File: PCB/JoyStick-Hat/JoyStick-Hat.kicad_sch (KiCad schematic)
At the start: 0 parts

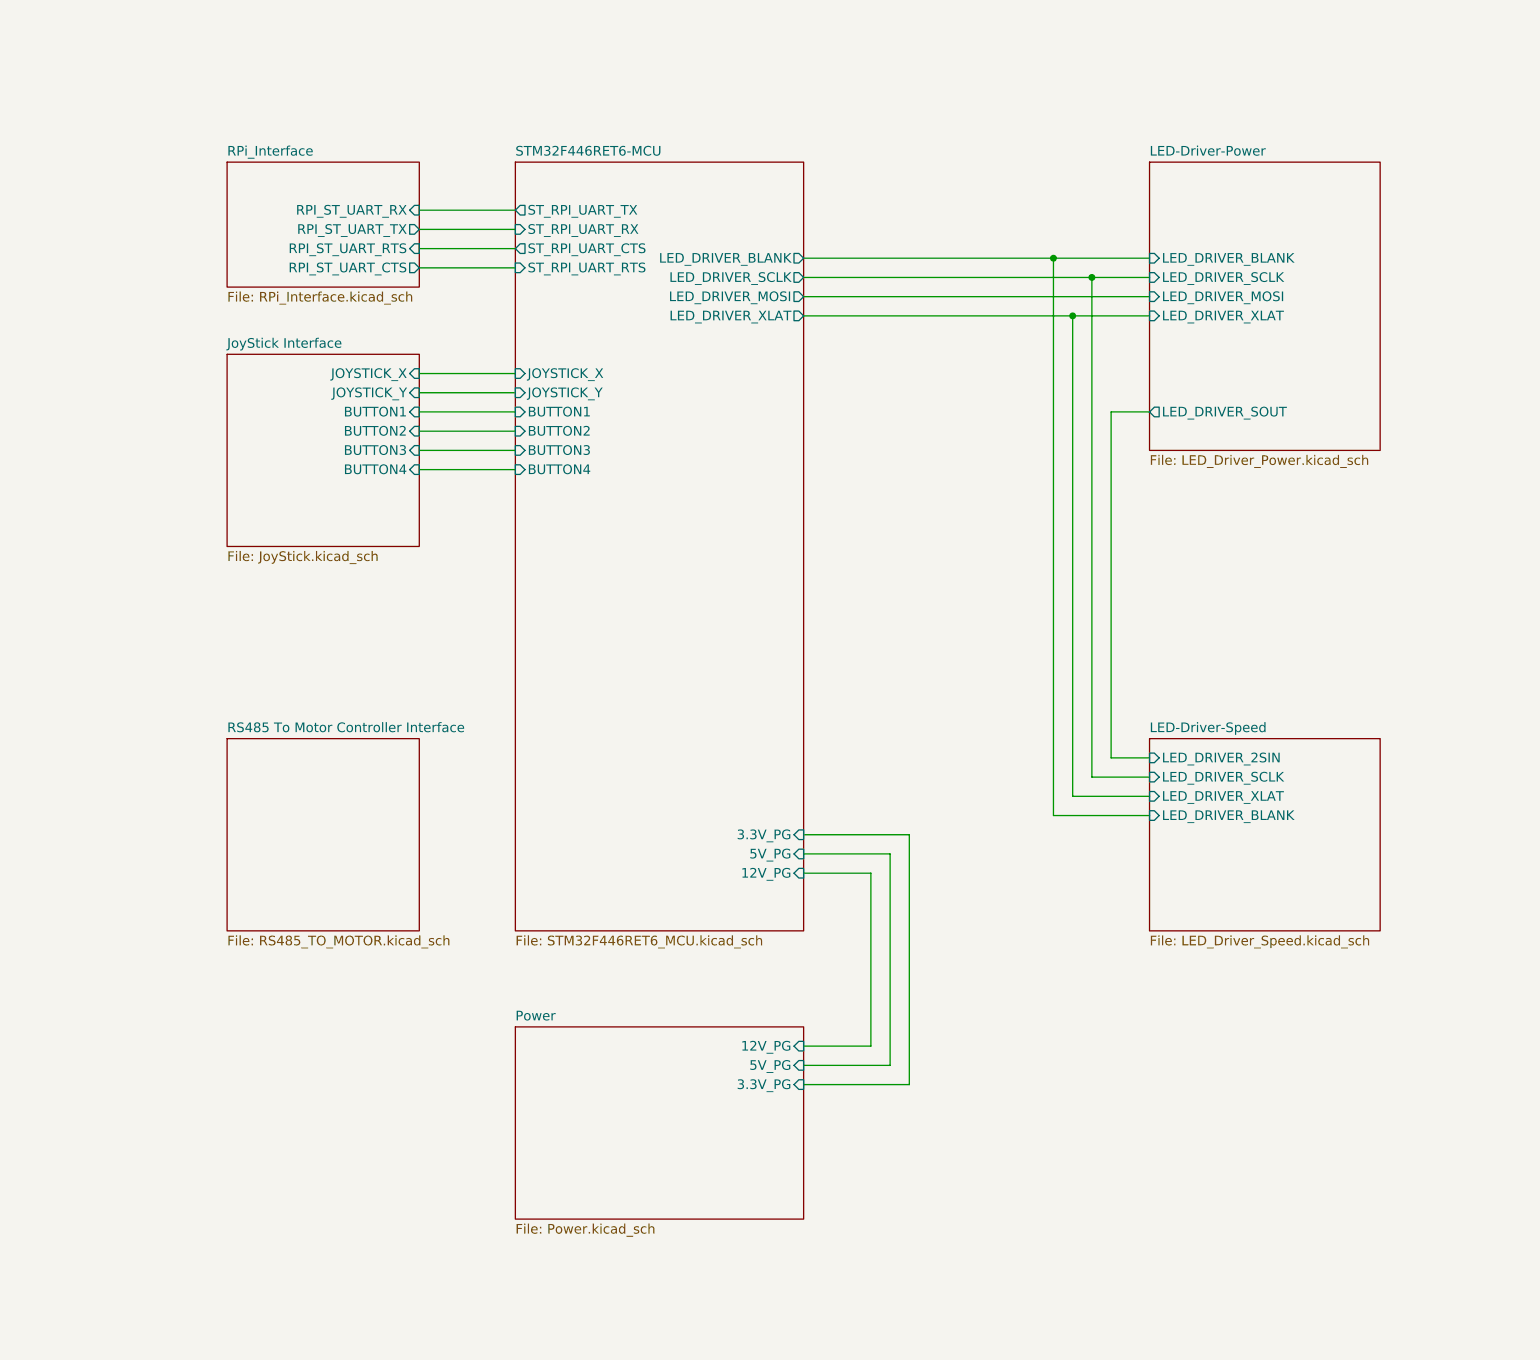
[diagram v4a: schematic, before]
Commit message: Schematic Complete
Schematic completed. Moved to 100 pin version of STM32 MCU for more connectivity and better muxing of internal peripherals with pins.
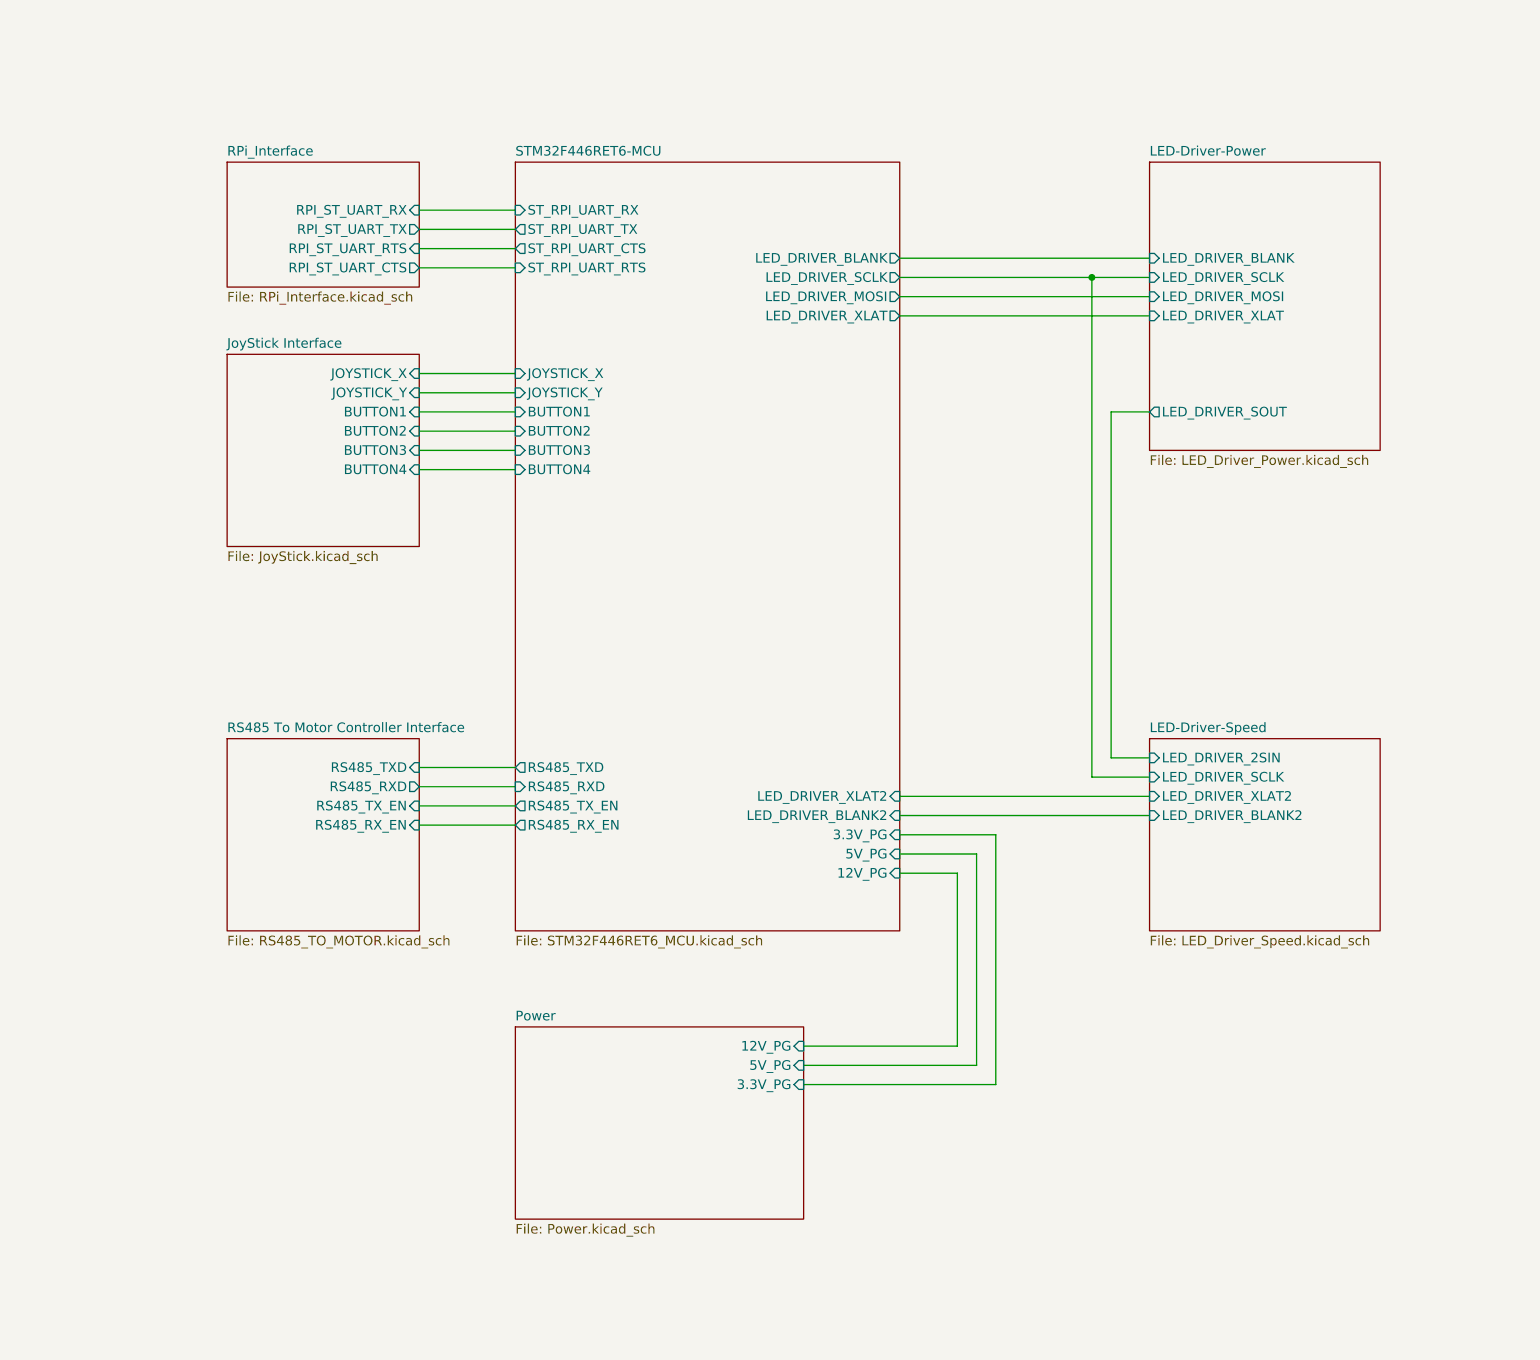
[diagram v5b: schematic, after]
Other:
- sheet LED-Driver-Speed ports: added LED_DRIVER_BLANK2, LED_DRIVER_XLAT2; removed LED_DRIVER_BLANK, LED_DRIVER_XLAT
- sheet RS485 To Motor Controller Interface ports: added RS485_RXD, RS485_RX_EN, RS485_TXD, RS485_TX_EN; removed none
- sheet STM32F446RET6-MCU ports: added LED_DRIVER_BLANK2, LED_DRIVER_XLAT2, RS485_RXD, RS485_RX_EN, RS485_TXD, RS485_TX_EN; removed none

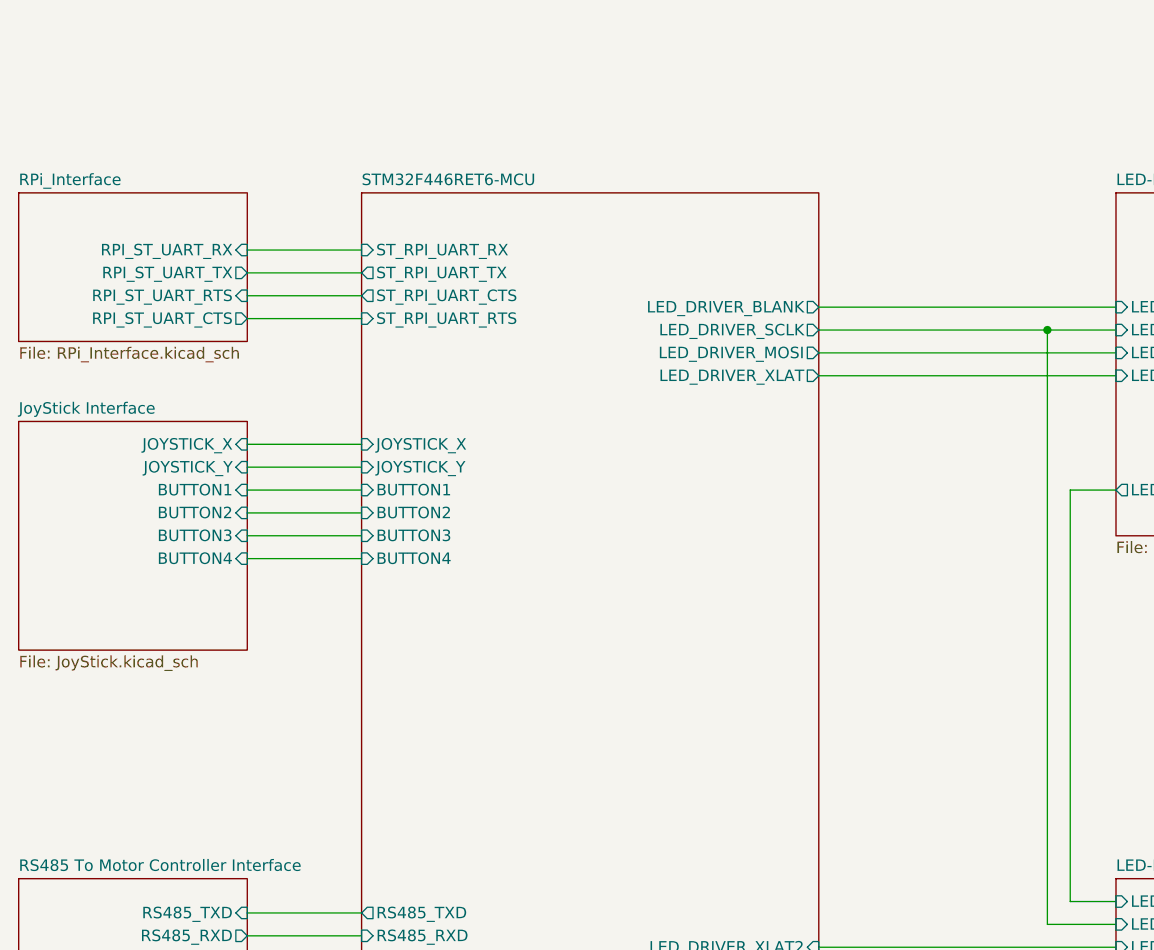
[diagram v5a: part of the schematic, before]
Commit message: LEDs and Additional connectors
Added heartbeat and diagnostic LEDs to STM32 and RPi3 schematics so we can directly flash them for debug purposes. Added a connector for serial port diagnostics on STM32. Added rotary switch interface for STM32 and added pullups to button connectors.
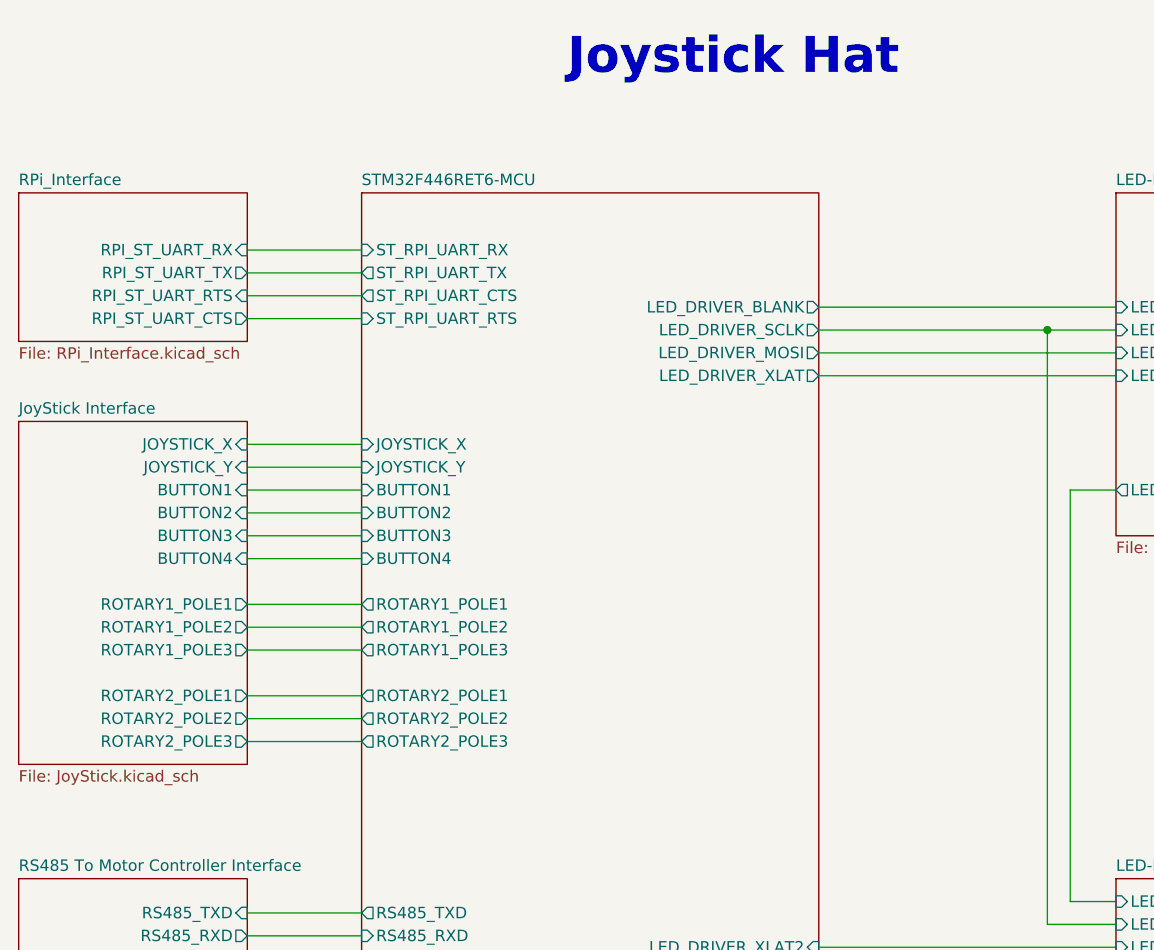
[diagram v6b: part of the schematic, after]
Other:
- sheet JoyStick Interface ports: added ROTARY1_POLE1, ROTARY1_POLE2, ROTARY1_POLE3, ROTARY2_POLE1, ROTARY2_POLE2, ROTARY2_POLE3; removed none
- sheet STM32F446RET6-MCU ports: added ROTARY1_POLE1, ROTARY1_POLE2, ROTARY1_POLE3, ROTARY2_POLE1, ROTARY2_POLE2, ROTARY2_POLE3; removed none
- note added: "Joystick Hat"
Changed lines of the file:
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@@
+    (stroke (width 0) (type default))
+  )
+  (wire (pts (xy 101.6 83.82) (xy 114.3 83.82))
     (stroke (width 0) (type default))
   )
@@
     (stroke (width 0) (type default))
   )
+  (wire (pts (xy 101.6 86.36) (xy 114.3 86.36))
+    (stroke (width 0) (type default))
+  )
   (wire (pts (xy 165.1 129.54) (xy 175.26 129.54))
     (stroke (width 0) (type default))
@@
     (stroke (width 0) (type default))
   )
+  (wire (pts (xy 101.6 99.06) (xy 114.3 99.06))
+    (stroke (width 0) (type default))
+  )
   (wire (pts (xy 101.6 118.11) (xy 114.3 118.11))
     (stroke (width 0) (type default))
@@
   (wire (pts (xy 165.1 53.34) (xy 190.5 53.34))
     (stroke (width 0) (type default))
+  )
+  (wire (pts (xy 101.6 88.9) (xy 114.3 88.9))
+    (stroke (width 0) (type default))
+  )
+  (wire (pts (xy 101.6 93.98) (xy 114.3 93.98))
+    (stroke (width 0) (type default))
+  )
+  (wire (pts (xy 101.6 96.52) (xy 114.3 96.52))
+    (stroke (width 0) (type default))
+  )
+  (text "Joystick Hat" (at 137.16 25.4 0)
+    (effects (font (size 4 4) (thickness 0.8) bold) (justify left bottom))
   )
   (sheet (at 198.12 114.3) (size 30.48 25.4) (fields_autoplaced)
@@
     )
   )
-  (sheet (at 76.2 63.5) (size 25.4 25.4) (fields_autoplaced)
+  (sheet (at 76.2 63.5) (size 25.4 38.1) (fields_autoplaced)
     (stroke (width 0.1524) (type solid))
     (fill (color 255 0 255 1.0000))
@@
       (effects (font (size 1.27 1.27)) (justify left bottom))
     )
-    (property "Sheetfile" "JoyStick.kicad_sch" (at 76.2 89.4846 0)
+    (property "Sheetfile" "JoyStick.kicad_sch" (at 76.2 102.1846 0)
       (effects (font (size 1.27 1.27)) (justify left top))
     )
@@
     )
     (pin "BUTTON1" input (at 101.6 71.12 0)
+      (effects (font (size 1.27 1.27)) (justify right))
+    )
+    (pin "ROTARY2_POLE1" output (at 101.6 93.98 0)
+      (effects (font (size 1.27 1.27)) (justify right))
+    )
+    (pin "ROTARY1_POLE2" output (at 101.6 86.36 0)
+      (effects (font (size 1.27 1.27)) (justify right))
+    )
+    (pin "ROTARY2_POLE3" output (at 101.6 99.06 0)
+      (effects (font (size 1.27 1.27)) (justify right))
+    )
+    (pin "ROTARY1_POLE1" output (at 101.6 83.82 0)
+      (effects (font (size 1.27 1.27)) (justify right))
+    )
+    (pin "ROTARY2_POLE2" output (at 101.6 96.52 0)
+      (effects (font (size 1.27 1.27)) (justify right))
+    )
+    (pin "ROTARY1_POLE3" output (at 101.6 88.9 0)
       (effects (font (size 1.27 1.27)) (justify right))
     )
@@
       (effects (font (size 1.27 1.27)) (justify left))
     )
+    (pin "ROTARY2_POLE3" output (at 114.3 99.06 180)
+      (effects (font (size 1.27 1.27)) (justify left))
+    )
+    (pin "ROTARY1_POLE1" output (at 114.3 83.82 180)
+      (effects (font (size 1.27 1.27)) (justify left))
+    )
+    (pin "ROTARY1_POLE2" output (at 114.3 86.36 180)
+      (effects (font (size 1.27 1.27)) (justify left))
+    )
+    (pin "ROTARY1_POLE3" output (at 114.3 88.9 180)
+      (effects (font (size 1.27 1.27)) (justify left))
+    )
+    (pin "ROTARY2_POLE2" output (at 114.3 96.52 180)
+      (effects (font (size 1.27 1.27)) (justify left))
+    )
+    (pin "ROTARY2_POLE1" output (at 114.3 93.98 180)
+      (effects (font (size 1.27 1.27)) (justify left))
+    )
